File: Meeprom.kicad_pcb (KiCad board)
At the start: 2 copper layers, 16 x 38 mm, 4 parts, among them J1 Molex 8878 socket 27C256 pino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, U1 28C256

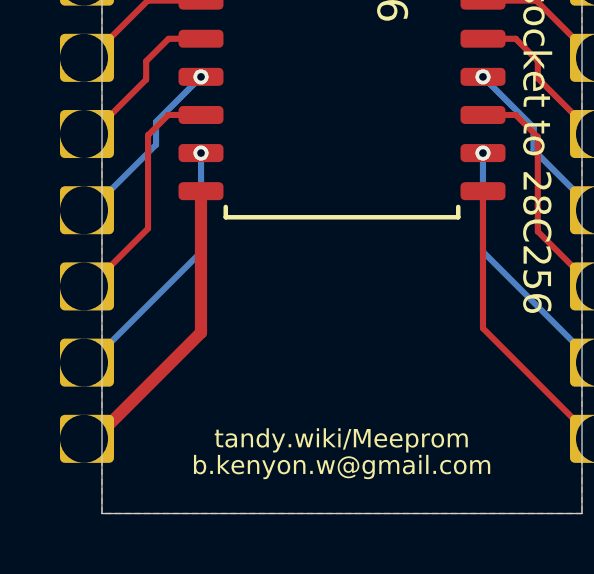
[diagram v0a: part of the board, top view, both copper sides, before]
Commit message: gitignore, remove explicit gnd trace
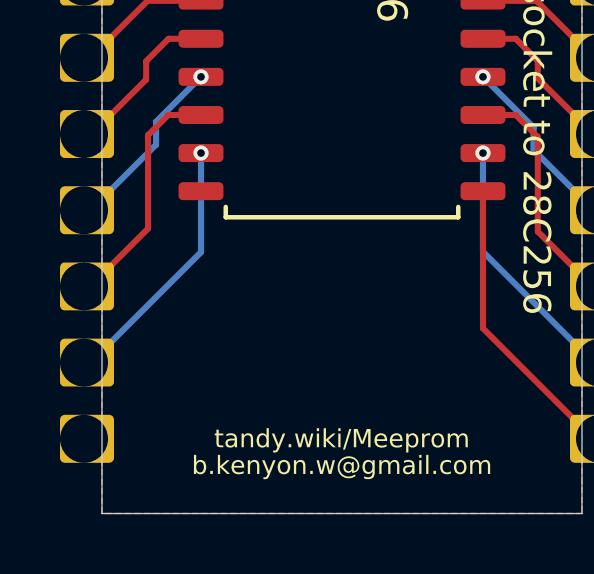
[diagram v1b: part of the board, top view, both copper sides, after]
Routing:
- net /VSS: track 9.99 -> 0.00 mm

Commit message: minor
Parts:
- R1: footprint Resistors_SMD:R_0805 -> 000_LOCAL:R_0805_2012Metric

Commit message: cosmetics
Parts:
- removed carrier?: pcb2molex8878_chamfer, 000_LOCAL:pcb2molex8878_chamfer
- J1: value Molex 8878 socket 27C256 pinout -> Molex 78805 socket 27C256 pinout; footprint 000_LOCAL:pcb2molex8878 -> 000_LOCAL:Molex78805_PCB
- R1: footprint 000_LOCAL:R_0805_2012Metric -> 000_LOCAL:R_0805
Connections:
- net /VCC renamed VCC
- J1 pad 14: /VSS -> (no net)
- U1 pad 14: /VSS -> (no net)
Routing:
- net (no net): track 0.00 -> 9.95 mm
- net /A14: track 15.7 -> 20.1 mm, vias 1 -> 0
- net /A13: track 7.44 -> 8.12 mm, vias 1 -> 0
- net /~WE: track 5.84 -> 5.19 mm
- net /A6: track 6.08 -> 6.40 mm, vias 1 -> 0
- net /D4: track 8.63 -> 8.94 mm, vias 1 -> 0
- net /D6: track 6.09 -> 6.40 mm, vias 1 -> 0
- net /D0: track 6.10 -> 6.40 mm, vias 1 -> 0
- net /D2: track 8.64 -> 8.91 mm, vias 1 -> 0
- net /A12: track 8.71 -> 8.94 mm, vias 1 -> 0
- net /VSS: vias 1 -> 0
- removed copper zone on B.Cu, net /VSS
- removed copper zone on F.Cu, net /VSS
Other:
- board size 16 x 38 mm -> 16.5 x 38 mm
- net class Default: clearance 0.2032 -> 0.2; trace_width 0.2032 -> 0.2; via_dia 0.508 -> 0.5; via_drill 0.254 -> 0.3
- rule trace_clearance: 0.2032 -> 0.2
- rule trace_min: 0.1524 -> 0.2
- rule via_min_drill: 0.254 -> 0.3
- rule via_min_size: 0.508 -> 0.5
- board text added: "28C256 to Molex 78805 socket 27C256 pinout"
- board text added: "Epson PX-4, PX-8"
- board text added: "FOR"
- board text added: "NOT FOR"
- board text added: "TANDY Model 102, 200"
- board text added: "TANDY Model 600"
- board text added: "TRS-80 Model 100"
- board text added: "Use with carrier: http://shpws.me/RqW3"
- board text added: "github.com/bkw777/Teeprom"
- board text removed: "27C256 pinout Molex socket to 28C256"
- board text removed: "Use with thingiverse.com/thing:3821586"
- board text removed: "b.kenyon.w@gmail.com"
- board text removed: "tandy.wiki/Meeprom"

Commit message: update to v004 board outline and carrier
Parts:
- J1: footprint 000_LOCAL:Molex78805_PCB -> 000_LOCAL:Molex78802_PCB_28
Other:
- board size 16.5 x 38 mm -> 16.6 x 38 mm
- board text added: "v004"

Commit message: silkscreens
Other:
- board text added: "27C256 pinout"
- board text added: "28C256 to Molex 78805 socket, 27C256 pinout"
- board text added: "Carrier: Molex78802_PCB_28 v004"
- board text added: "NOT for TRS-80/TANDY Model 100, 102, 200"
- board text added: "tandy.wiki/Meeprom v004"
- board text removed: "27C256"
- board text removed: "28C256 to Molex 78805 socket 27C256 pinout"
- board text removed: "Epson PX-4, PX-8"
- board text removed: "FOR"
- board text removed: "NOT FOR"
- board text removed: "TANDY Model 102, 200"
- board text removed: "TANDY Model 600"
- board text removed: "TRS-80 Model 100"
- board text removed: "Use with carrier: http://shpws.me/RqW3"
- board text removed: "github.com/bkw777/Teeprom"
- board text removed: "v004"

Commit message: add MEE2732
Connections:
- J1 pad 14: (no net) -> GND
- U1 pad 14: (no net) -> GND
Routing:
- net GND: track 0.00 -> 9.95 mm
- net (no net): track 9.95 -> 0.00 mm

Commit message: spurious leftover trace on Meeprom
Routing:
- net /A9: track 6.07 -> 5.17 mm

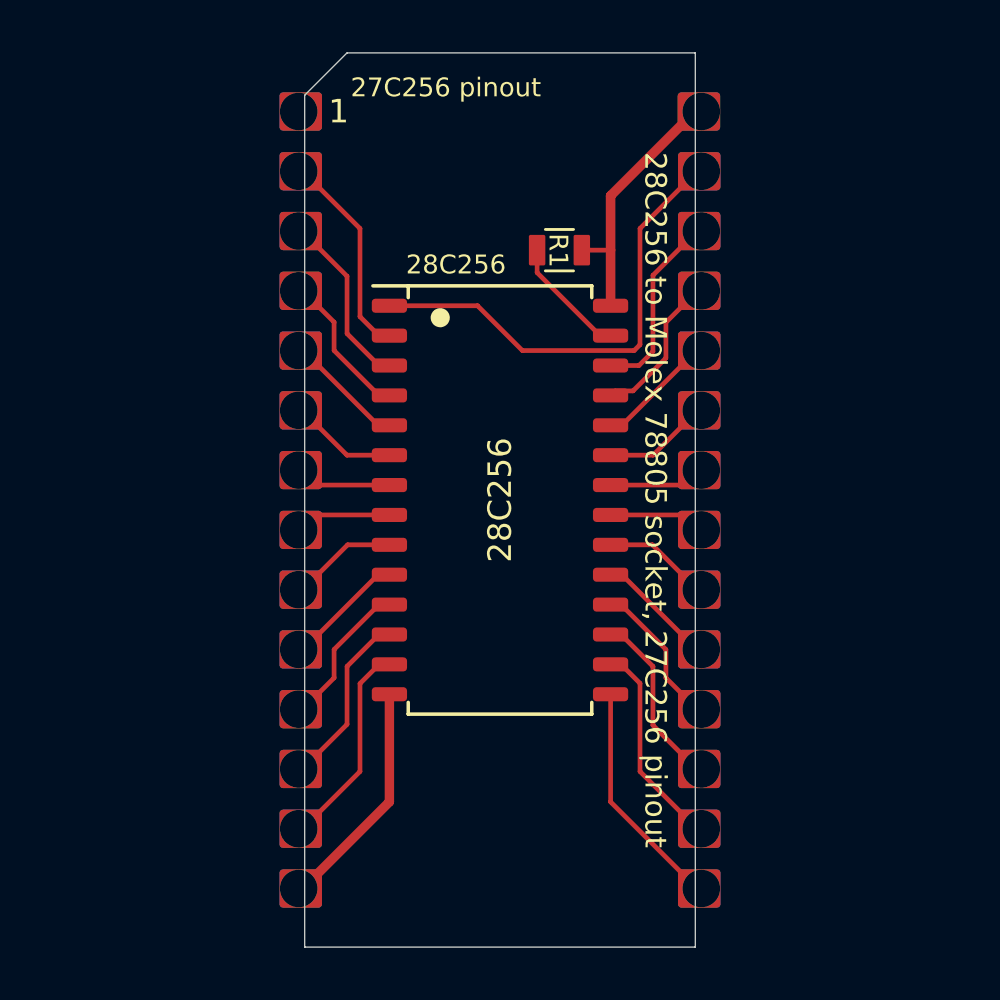
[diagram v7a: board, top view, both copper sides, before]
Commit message: kicad 6, flashopt100 programming socket
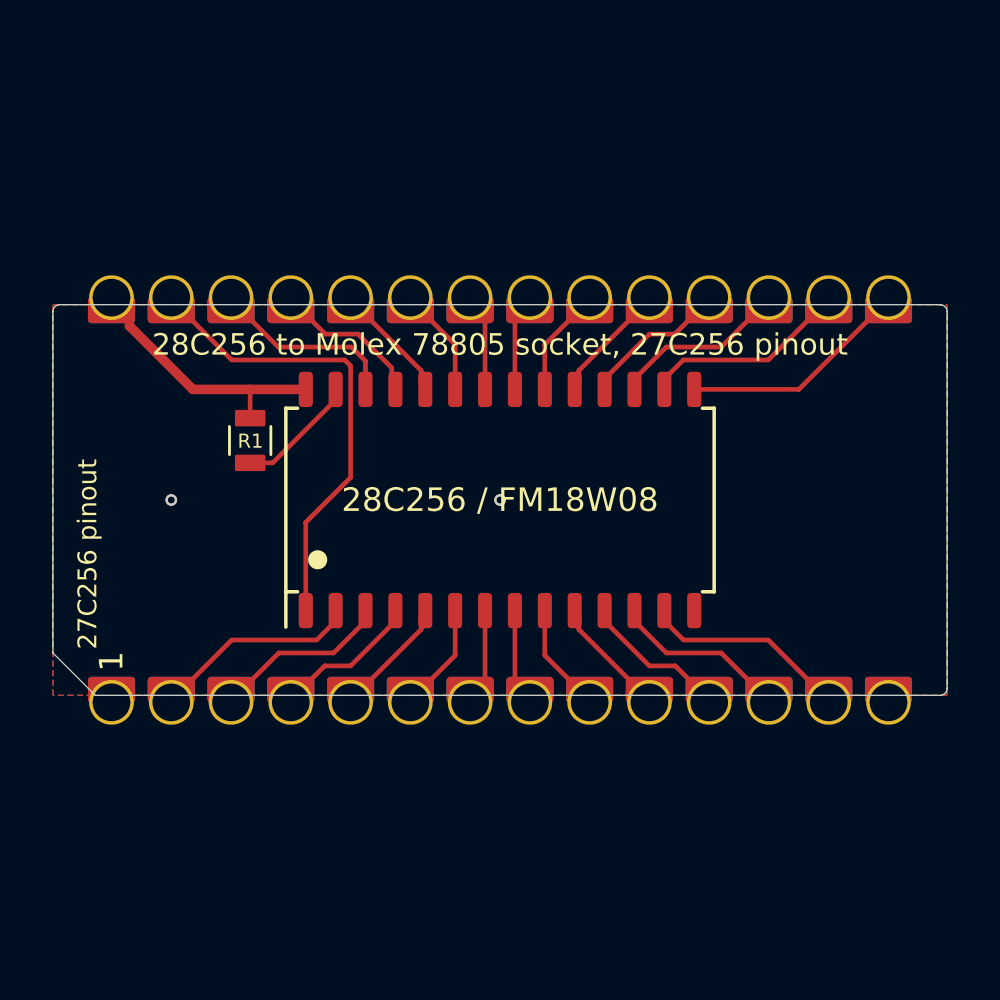
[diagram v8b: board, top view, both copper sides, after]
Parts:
- J1: value Molex 78805 socket 27C256 pinout -> Molex 78805 socket with 27C256 pinout
- U1: value 28C256 -> 28C256 / FM18W08
- moved R1 15.4 mm to (136.6, 96.7), turned to 90 degrees
- turned J1 to 90 degrees
- turned U1 to 90 degrees
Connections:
- net /~CE renamed /~{CE}
- net /~OE renamed /~{OE}
- net /~WE renamed /~{WE}
- J1 pad 1: (no net) -> unconnected-(J1-Pad1)
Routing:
- net GND: track 9.95 -> 0.00 mm, vias 0 -> 2
- net /A3: track 4.13 -> 4.70 mm
- added copper zone on B.Cu, net GND
- added copper zone on F.Cu, net GND
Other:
- board size 16.6 x 38 mm -> 38 x 16.6 mm
- net class Default removed
- board text added: "${TITLE} ${REVISION} ${COMMENT2}"
- board text added: "R1: ${00000000-0000-0000-0000-00005d22c129:VALUE} Use Carrier: Molex78802_PCB_28 v004"
- board text removed: "28C256"
- board text removed: "Carrier: Molex78802_PCB_28 v004"
- board text removed: "R1: 47k"
- board text removed: "tandy.wiki/Meeprom v004"
